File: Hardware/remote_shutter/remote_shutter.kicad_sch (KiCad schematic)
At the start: 0 parts

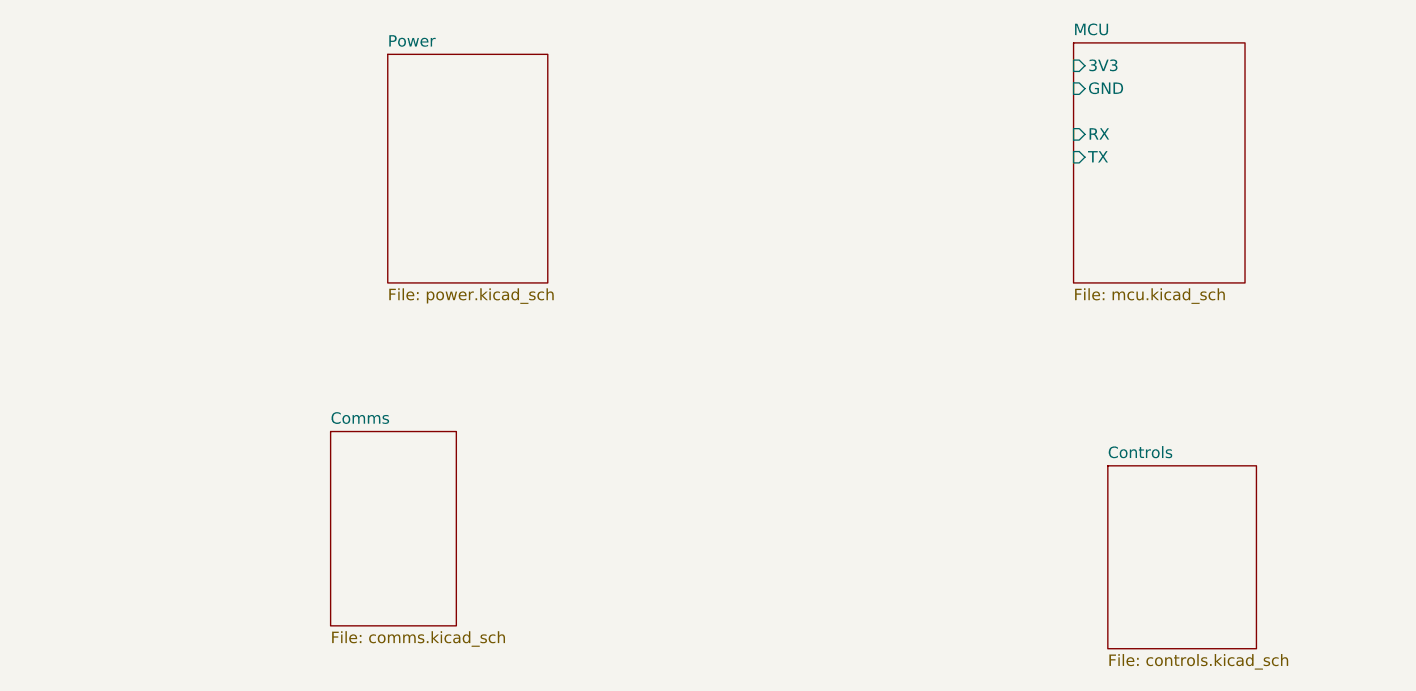
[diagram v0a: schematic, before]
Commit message: Added BOM. Added controls.
Placed jack, switches, OLED display and rotary encoders.
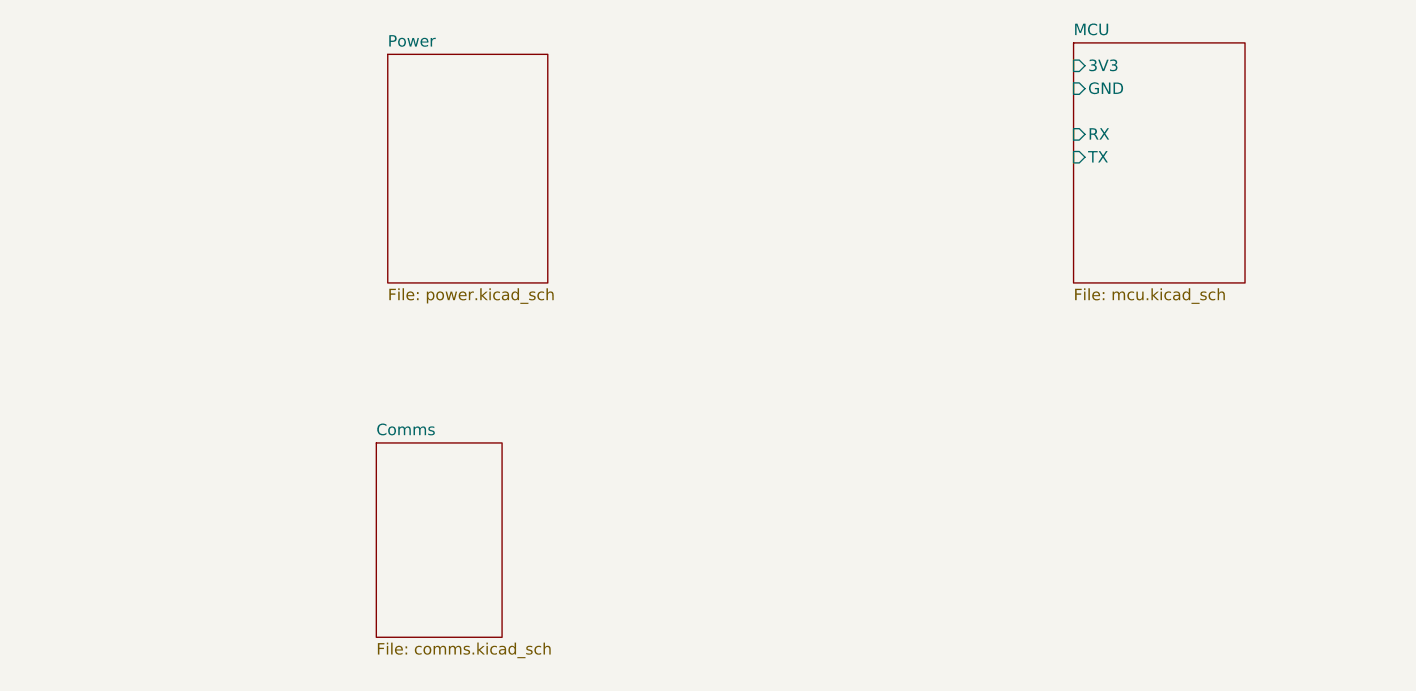
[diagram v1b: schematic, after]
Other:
- removed sheet Controls
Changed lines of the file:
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@@
     )
   )
-  (sheet (at 83.82 107.95) (size 13.97 21.59) (fields_autoplaced)
+  (sheet (at 88.9 109.22) (size 13.97 21.59) (fields_autoplaced)
     (stroke (width 0.1524) (type solid) (color 0 0 0 0))
     (fill (color 255 229 191 1.0000))
-    (property "Sheet name" "Comms" (id 0) (at 83.82 107.2384 0)
+    (property "Sheet name" "Comms" (id 0) (at 88.9 108.5084 0)
       (effects (font (size 1.27 1.27)) (justify left bottom))
     )
-    (property "Sheet file" "comms.kicad_sch" (id 1) (at 83.82 130.1246 0)
-      (effects (font (size 1.27 1.27)) (justify left top))
-    )
-  )
-  (sheet (at 170.18 111.76) (size 16.51 20.32) (fields_autoplaced)
-    (stroke (width 0.1524) (type solid) (color 0 0 0 0))
-    (fill (color 255 229 191 1.0000))
-    (property "Sheet name" "Controls" (id 0) (at 170.18 111.0484 0)
-      (effects (font (size 1.27 1.27)) (justify left bottom))
-    )
-    (property "Sheet file" "controls.kicad_sch" (id 1) (at 170.18 132.6646 0)
+    (property "Sheet file" "comms.kicad_sch" (id 1) (at 88.9 131.3946 0)
       (effects (font (size 1.27 1.27)) (justify left top))
     )
@@
     (path "/" (page "1"))
     (path "/0c902a43-b121-4fe4-bfa1-34ed8f238e77" (page "2"))
-    (path "/3fcd1df3-7d81-48ad-8dea-5392cbaac6cf" (page "3"))
+    (path "/76614985-77bf-4b33-94c5-94a8e5c748f5/44fe3afb-1c9a-46d5-8310-2d9db6eb3664" (page "3"))
     (path "/76614985-77bf-4b33-94c5-94a8e5c748f5" (page "4"))
     (path "/3dcb1c41-c4c6-4f4e-893c-6da19846cf43" (page "5"))
   )
   (symbol_instances
+    (path "/76614985-77bf-4b33-94c5-94a8e5c748f5/44fe3afb-1c9a-46d5-8310-2d9db6eb3664/dd70d261-10ac-488f-88aa-dc27e0cb0046"
+      (reference "#PWR?") (unit 1) (value "GND") (footprint "")
+    )
+    (path "/76614985-77bf-4b33-94c5-94a8e5c748f5/44fe3afb-1c9a-46d5-8310-2d9db6eb3664/6b37076e-d8fd-4af0-ac80-0898d34aa122"
+      (reference "J?") (unit 1) (value "Conn_01x08_Male") (footprint "Connector_PinSocket_2.54mm:PinSocket_1x08_P2.54mm_Vertical")
+    )
+    (path "/76614985-77bf-4b33-94c5-94a8e5c748f5/44fe3afb-1c9a-46d5-8310-2d9db6eb3664/c2aaade8-f811-4bfa-9ad0-c176bfc17150"
+      (reference "J?") (unit 1) (value "AudioJack3") (footprint "")
+    )
+    (path "/76614985-77bf-4b33-94c5-94a8e5c748f5/44fe3afb-1c9a-46d5-8310-2d9db6eb3664/7e48265c-802c-44ca-ba29-6fca3dd0ca2d"
+      (reference "Q?") (unit 1) (value "DMN2056U") (footprint "Package_TO_SOT_SMD:SOT-23")
+    )
+    (path "/76614985-77bf-4b33-94c5-94a8e5c748f5/44fe3afb-1c9a-46d5-8310-2d9db6eb3664/a7e9f57e-b0ff-40b7-88d8-79023fc30b72"
+      (reference "Q?") (unit 1) (value "DMN2056U") (footprint "Package_TO_SOT_SMD:SOT-23")
+    )
+    (path "/76614985-77bf-4b33-94c5-94a8e5c748f5/44fe3afb-1c9a-46d5-8310-2d9db6eb3664/4835f8a5-e52e-4e3d-a197-0a9ab9c36525"
+      (reference "S?") (unit 1) (value "4-1437565-2") (footprint "SW_4-1437565-2")
+    )
+    (path "/76614985-77bf-4b33-94c5-94a8e5c748f5/44fe3afb-1c9a-46d5-8310-2d9db6eb3664/9446ca53-3d1a-4bf9-9cc7-851a4093e407"
+      (reference "S?") (unit 1) (value "4-1437565-2") (footprint "SW_4-1437565-2")
+    )
+    (path "/76614985-77bf-4b33-94c5-94a8e5c748f5/44fe3afb-1c9a-46d5-8310-2d9db6eb3664/69e45d6e-f735-4840-a3df-e1eb732484f9"
+      (reference "SW?") (unit 1) (value "RotaryEncoder_Switch") (footprint "")
+    )
+    (path "/76614985-77bf-4b33-94c5-94a8e5c748f5/44fe3afb-1c9a-46d5-8310-2d9db6eb3664/9ac12d0a-be28-4401-a1e6-93cd4ca8cf3d"
+      (reference "SW?") (unit 1) (value "RotaryEncoder_Switch") (footprint "")
+    )
+    (path "/76614985-77bf-4b33-94c5-94a8e5c748f5/44fe3afb-1c9a-46d5-8310-2d9db6eb3664/dbe1cf3a-77c2-4b99-9184-428262e91ab4"
+      (reference "SW?") (unit 1) (value "RotaryEncoder_Switch") (footprint "")
+    )
     (path "/3dcb1c41-c4c6-4f4e-893c-6da19846cf43/0a7f7c39-bd34-4869-bd34-fc026b206fdc"
       (reference "U?") (unit 1) (value "CP2102N-Axx-xQFN24") (footprint "Package_DFN_QFN:QFN-24-1EP_4x4mm_P0.5mm_EP2.6x2.6mm")

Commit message: Added power & comms.
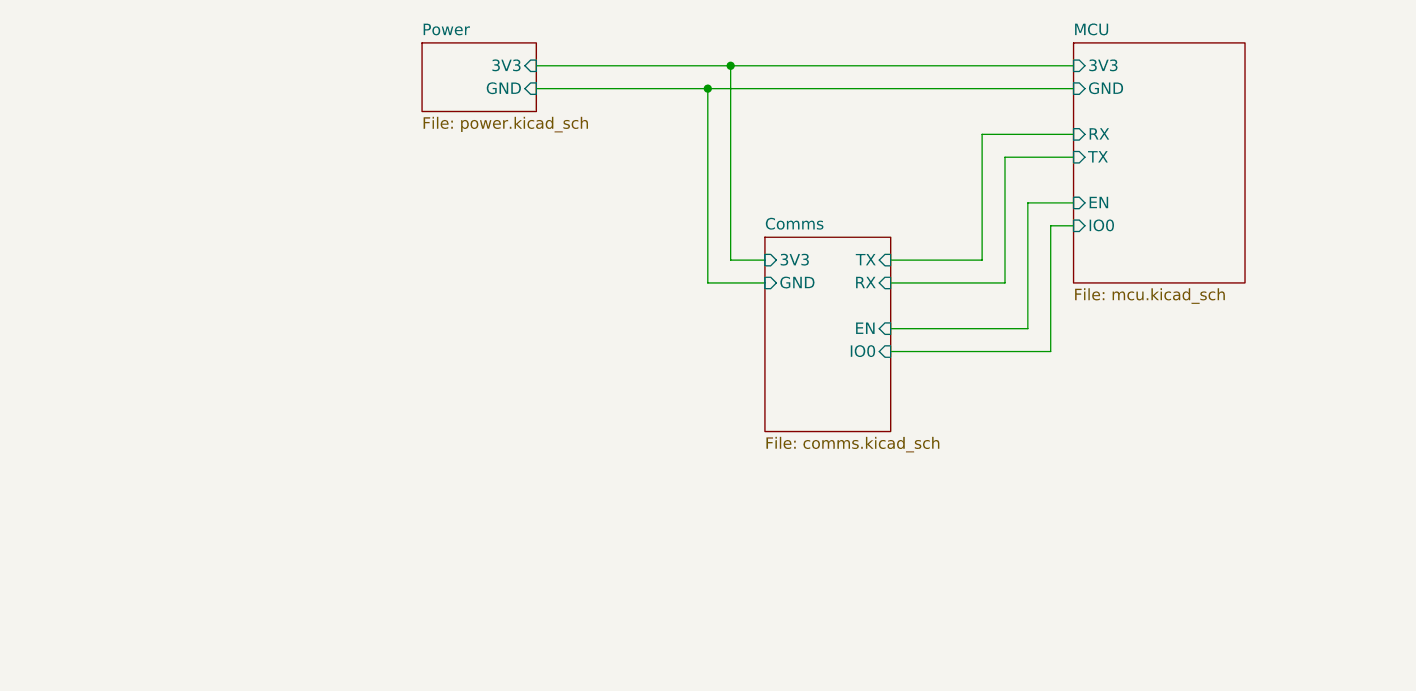
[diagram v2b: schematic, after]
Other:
- sheet Comms ports: added 3V3, EN, GND, IO0, RX, TX; removed none
- sheet MCU ports: added EN, IO0; removed none
- sheet Power ports: added 3V3, GND; removed none

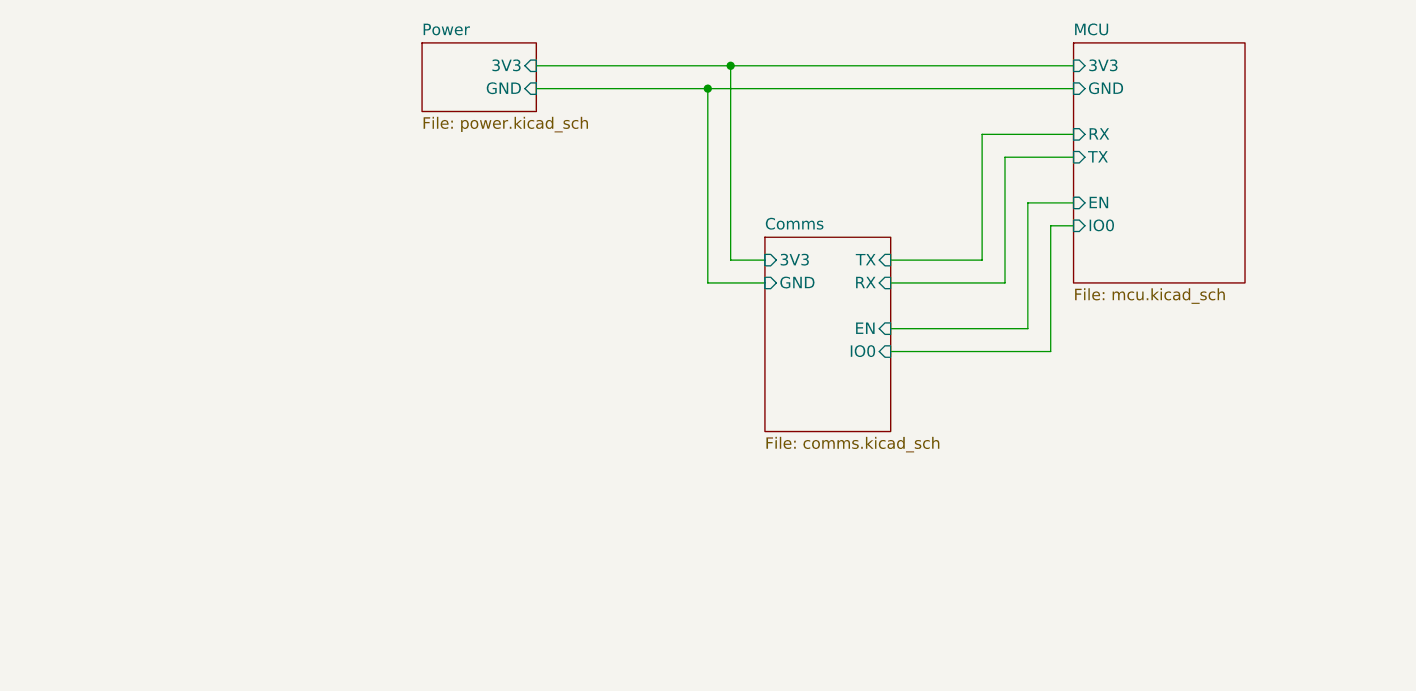
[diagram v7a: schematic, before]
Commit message: Added LiIon charge circuit
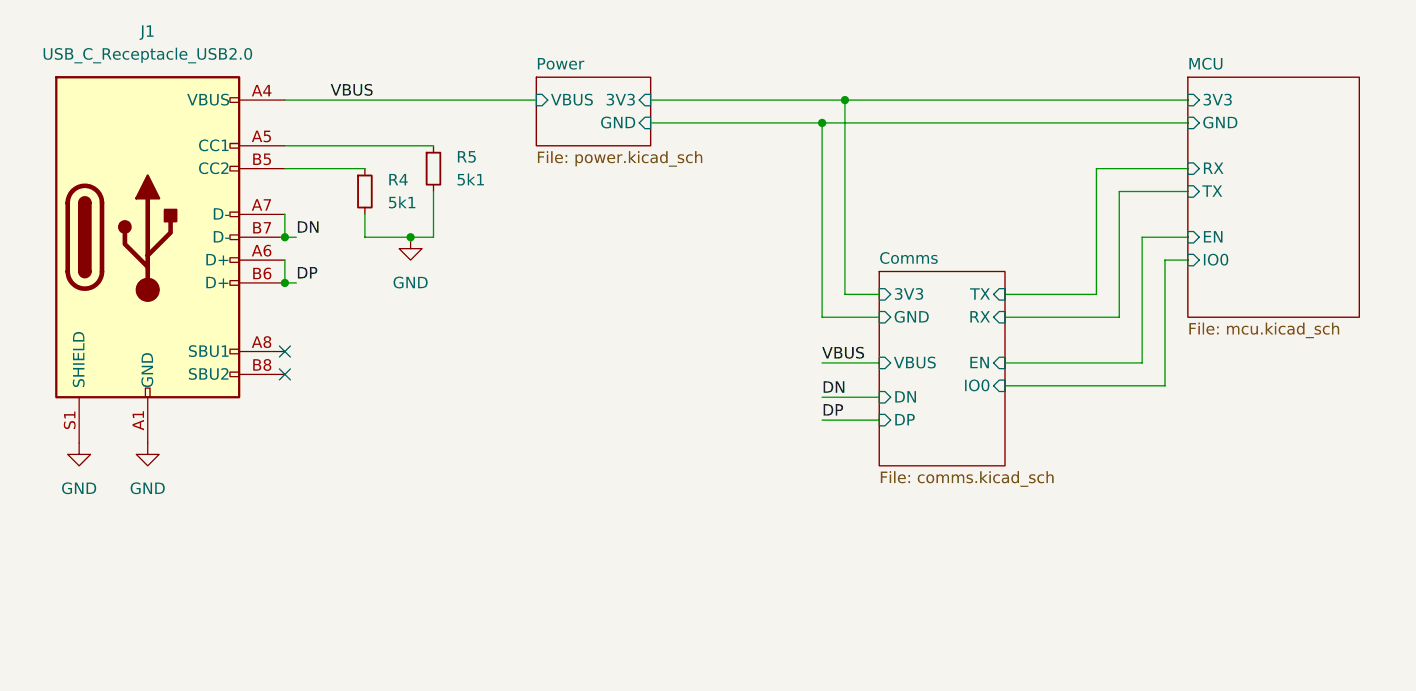
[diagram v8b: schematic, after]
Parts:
- added J1: USB_C_Receptacle_USB2.0, Connector_USB:USB_C_Receptacle_XKB_U262-16XN-4BVC11, symbol Connector:USB_C_Receptacle_USB2.0
- added R4, R5: 5k1, Resistor_SMD:R_0603_1608Metric_Pad0.98x0.95mm_HandSolder, symbol Device:R_Small
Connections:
- new net: J1.A5 (CC1), R5.1
- new net: J1.B5 (CC2), R4.1
- new net DN: J1.A7 (D-), J1.B7 (D-)
- new net DP: J1.A6 (D+), J1.B6 (D+)
- new net GND: J1.A1 (GND), J1.A12 (GND), J1.B1 (GND), J1.B12 (GND), J1.S1 (SHIELD), R4.2, R5.2
- new net VBUS: J1.A4 (VBUS), J1.A9 (VBUS), J1.B4 (VBUS), J1.B9 (VBUS)
- no-connect marks 0 -> 2
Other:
- sheet Comms ports: added DN, DP, VBUS; removed none
- sheet Power ports: added VBUS; removed none
